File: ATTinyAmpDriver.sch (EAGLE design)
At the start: 22 parts, among them Q1 BSP100, U1 SPX5205M5-L-3-3, U2 ATTINY5-TSHR, U3 MCP6001, X1 DIODES, X2 INPUT

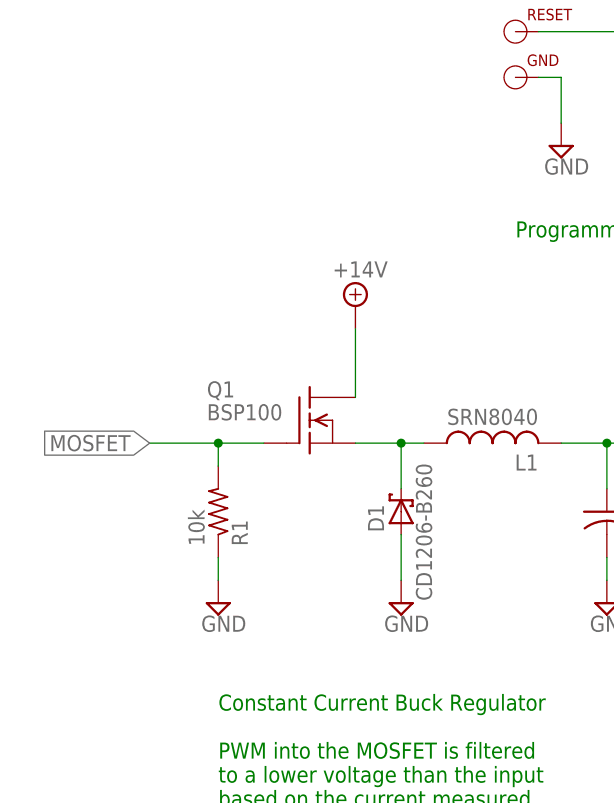
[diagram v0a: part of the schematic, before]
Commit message: P Channel MOSFET
Changed from Incorrect N-Channel to P-Channel High side switch on the
Driver Circuit.
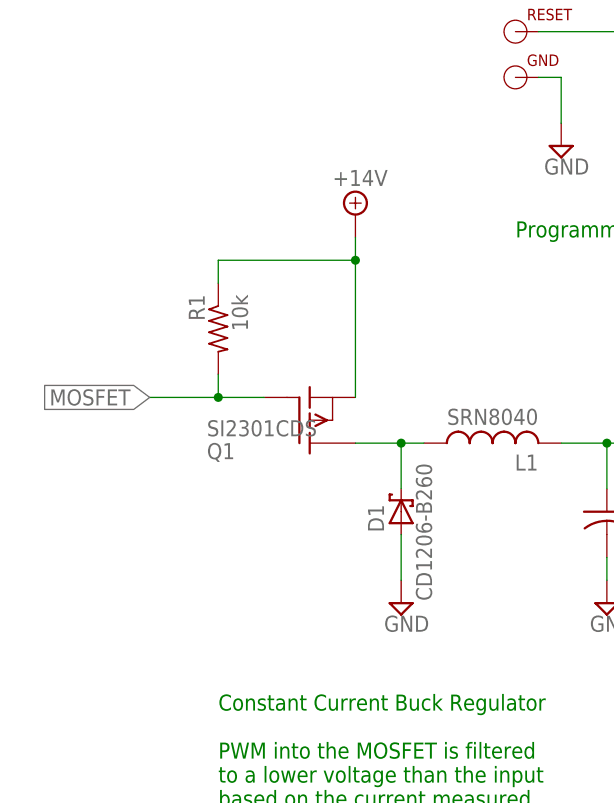
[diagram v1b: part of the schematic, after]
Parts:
- Q1: value BSP100 -> SI2301CDS; device Personal:BSP100 -> Combined:SI2301CDS
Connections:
- net +14V: now also Q1.S, R1.1; no longer Q1.D
- net GND: no longer R1.1
- net L+: now also Q1.D; no longer Q1.S
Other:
- moved on the sheet: Q1, R1
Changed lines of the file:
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@@
 <part name="SUPPLY8" library="supply2" deviceset="GND" device=""/>
 <part name="X1" library="con-phoenix-254" deviceset="MPT2" device="" value="DIODES"/>
-<part name="Q1" library="Personal" deviceset="BSP100" device="">
+<part name="Q1" library="Combined" deviceset="SI2301CDS" device="">
 <attribute name="DIGIKEY" value="568-6956-1-ND"/>
 <attribute name="DIGIKEY_COST" value=".69"/>
@@
 <attribute name="DIGIKEY_COST" value=".05"/>
 </part>
-<part name="SUPPLY14" library="supply2" deviceset="GND" device=""/>
 <part name="TPIDATA" library="Personal" deviceset="TPI" device=""/>
 <part name="TPICLK" library="Personal" deviceset="TPI" device=""/>
@@
 <instance part="X1" gate="-1" x="116.84" y="68.58"/>
 <instance part="X1" gate="-2" x="116.84" y="60.96"/>
-<instance part="Q1" gate="G$1" x="66.04" y="71.12">
-<attribute name="DIGIKEY" x="66.04" y="71.12" size="1.778" layer="96" display="off"/>
-<attribute name="DIGIKEY_COST" x="66.04" y="71.12" size="1.778" layer="96" display="off"/>
-</instance>
-<instance part="SUPPLY11" gate="G$1" x="71.12" y="83.82"/>
+<instance part="Q1" gate="G$1" x="66.04" y="71.12" rot="MR180">
+<attribute name="DIGIKEY" x="66.04" y="71.12" size="1.778" layer="96" rot="MR180" display="off"/>
+<attribute name="DIGIKEY_COST" x="66.04" y="71.12" size="1.778" layer="96" rot="MR180" display="off"/>
+</instance>
+<instance part="SUPPLY11" gate="G$1" x="71.12" y="93.98"/>
 <instance part="U2" gate="A" x="187.96" y="182.88">
 <attribute name="DIGIKEY" x="187.96" y="182.88" size="1.778" layer="96" display="off"/>
@@
 </instance>
 <instance part="SUPPLY13" gate="GND" x="99.06" y="50.8"/>
-<instance part="R1" gate="G$1" x="55.88" y="60.96" rot="MR90">
-<attribute name="DIGIKEY" x="55.88" y="60.96" size="1.778" layer="96" rot="MR90" display="off"/>
-<attribute name="DIGIKEY_COST" x="55.88" y="60.96" size="1.778" layer="96" rot="MR90" display="off"/>
-</instance>
-<instance part="SUPPLY14" gate="GND" x="55.88" y="50.8"/>
+<instance part="R1" gate="G$1" x="55.88" y="81.28" rot="MR270">
+<attribute name="DIGIKEY" x="55.88" y="81.28" size="1.778" layer="96" rot="MR270" display="off"/>
+<attribute name="DIGIKEY_COST" x="55.88" y="81.28" size="1.778" layer="96" rot="MR270" display="off"/>
+</instance>
 <instance part="TPIDATA" gate="G$1" x="88.9" y="124.46"/>
 <instance part="TPICLK" gate="G$1" x="88.9" y="119.38"/>
@@
 </segment>
 <segment>
-<pinref part="R1" gate="G$1" pin="1"/>
-<pinref part="SUPPLY14" gate="GND" pin="GND"/>
-<wire x1="55.88" y1="55.88" x2="55.88" y2="53.34" width="0.1524" layer="91"/>
-</segment>
-<segment>
 <pinref part="GND" gate="G$1" pin="TPI_PIN"/>
 <pinref part="SUPPLY16" gate="GND" pin="GND"/>
@@
 </segment>
 <segment>
-<pinref part="Q1" gate="G$1" pin="D"/>
 <pinref part="SUPPLY11" gate="G$1" pin="+14V"/>
-<wire x1="71.12" y1="73.66" x2="71.12" y2="81.28" width="0.1524" layer="91"/>
+<pinref part="Q1" gate="G$1" pin="S"/>
+<wire x1="71.12" y1="91.44" x2="71.12" y2="88.9" width="0.1524" layer="91"/>
+<pinref part="R1" gate="G$1" pin="1"/>
+<wire x1="71.12" y1="88.9" x2="71.12" y2="73.66" width="0.1524" layer="91"/>
+<wire x1="55.88" y1="86.36" x2="55.88" y2="88.9" width="0.1524" layer="91"/>
+<wire x1="55.88" y1="88.9" x2="71.12" y2="88.9" width="0.1524" layer="91"/>
+<junction x="71.12" y="88.9"/>
 </segment>
 </net>
@@
 <net name="MOSFET" class="0">
 <segment>
+<label x="48.26" y="73.66" size="1.778" layer="95" rot="R180" xref="yes"/>
+<pinref part="R1" gate="G$1" pin="2"/>
+<wire x1="55.88" y1="73.66" x2="48.26" y2="73.66" width="0.1524" layer="91"/>
+<wire x1="55.88" y1="76.2" x2="55.88" y2="73.66" width="0.1524" layer="91"/>
 <pinref part="Q1" gate="G$1" pin="G"/>
-<wire x1="60.96" y1="68.58" x2="55.88" y2="68.58" width="0.1524" layer="91"/>
-<label x="48.26" y="68.58" size="1.778" layer="95" rot="R180" xref="yes"/>
-<pinref part="R1" gate="G$1" pin="2"/>
-<wire x1="55.88" y1="68.58" x2="48.26" y2="68.58" width="0.1524" layer="91"/>
-<wire x1="55.88" y1="66.04" x2="55.88" y2="68.58" width="0.1524" layer="91"/>
-<junction x="55.88" y="68.58"/>
+<wire x1="60.96" y1="73.66" x2="55.88" y2="73.66" width="0.1524" layer="91"/>
+<junction x="55.88" y="73.66"/>
 </segment>
 <segment>
@@
 <pinref part="D1" gate="G$1" pin="C"/>
 <wire x1="76.2" y1="63.5" x2="76.2" y2="68.58" width="0.1524" layer="91"/>
-<pinref part="Q1" gate="G$1" pin="S"/>
-<wire x1="71.12" y1="68.58" x2="76.2" y2="68.58" width="0.1524" layer="91"/>
 <pinref part="L1" gate="G$1" pin="1"/>
 <wire x1="78.74" y1="68.58" x2="76.2" y2="68.58" width="0.1524" layer="91"/>
+<pinref part="Q1" gate="G$1" pin="D"/>
+<wire x1="71.12" y1="68.58" x2="76.2" y2="68.58" width="0.1524" layer="91"/>
 <junction x="76.2" y="68.58"/>
 </segment>

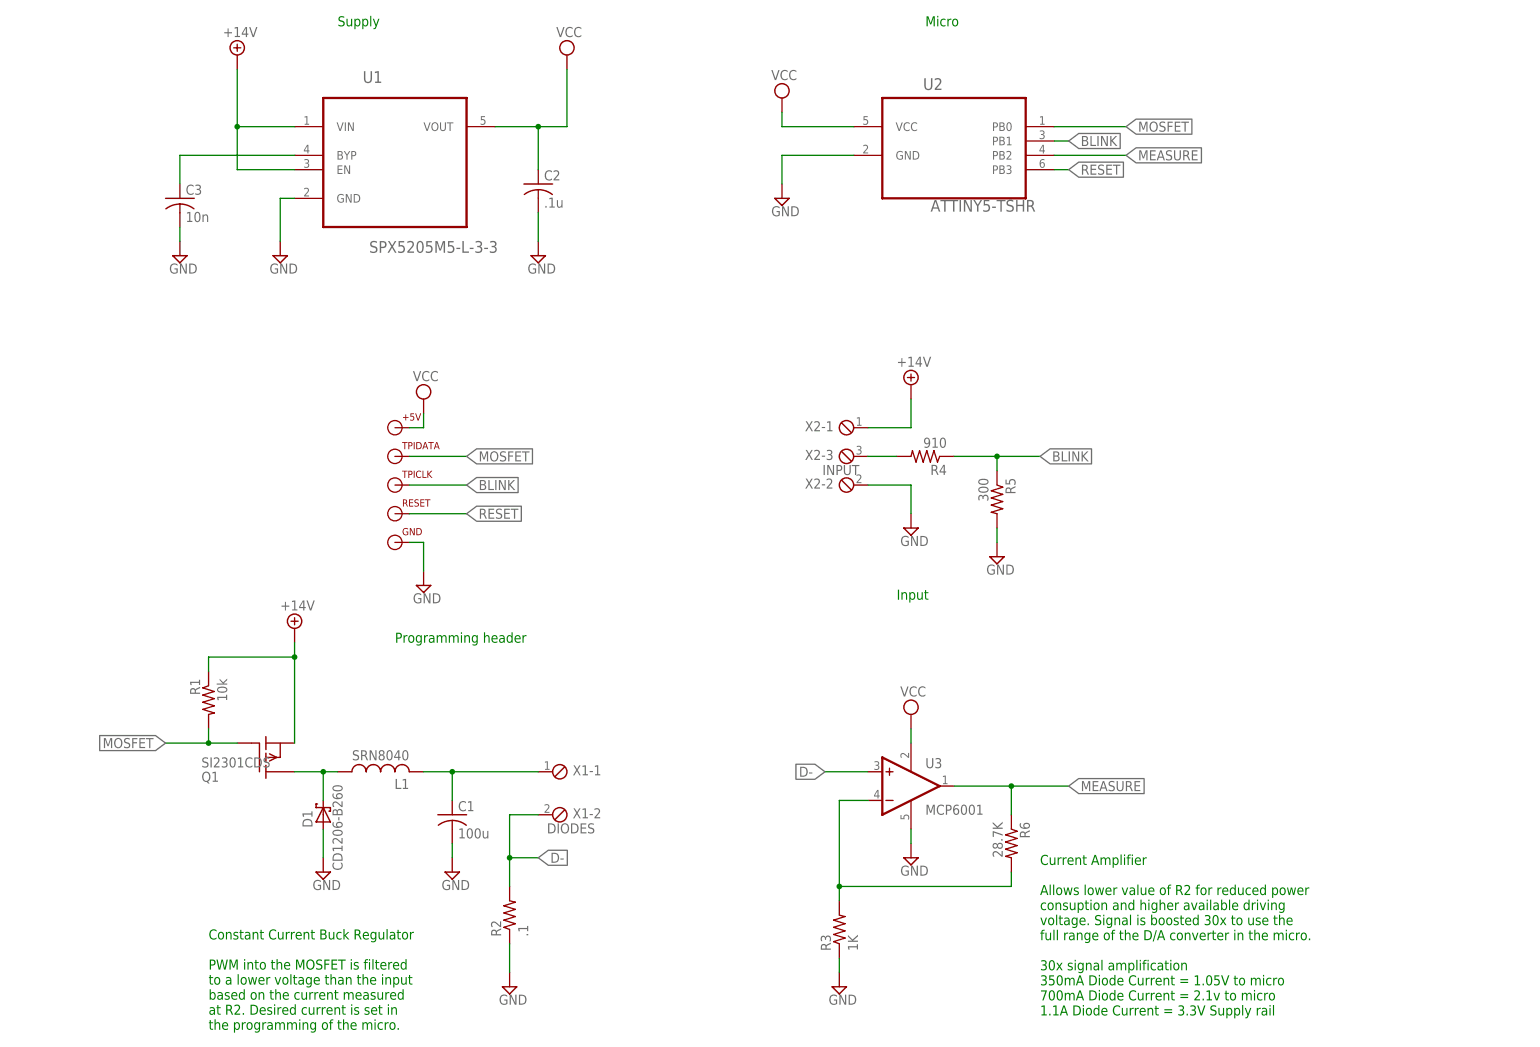
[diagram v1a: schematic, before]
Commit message: Added Driving transistor for P-FET
Added driver transistor to P Channel MOSFET and capacitor to op-amp
output.
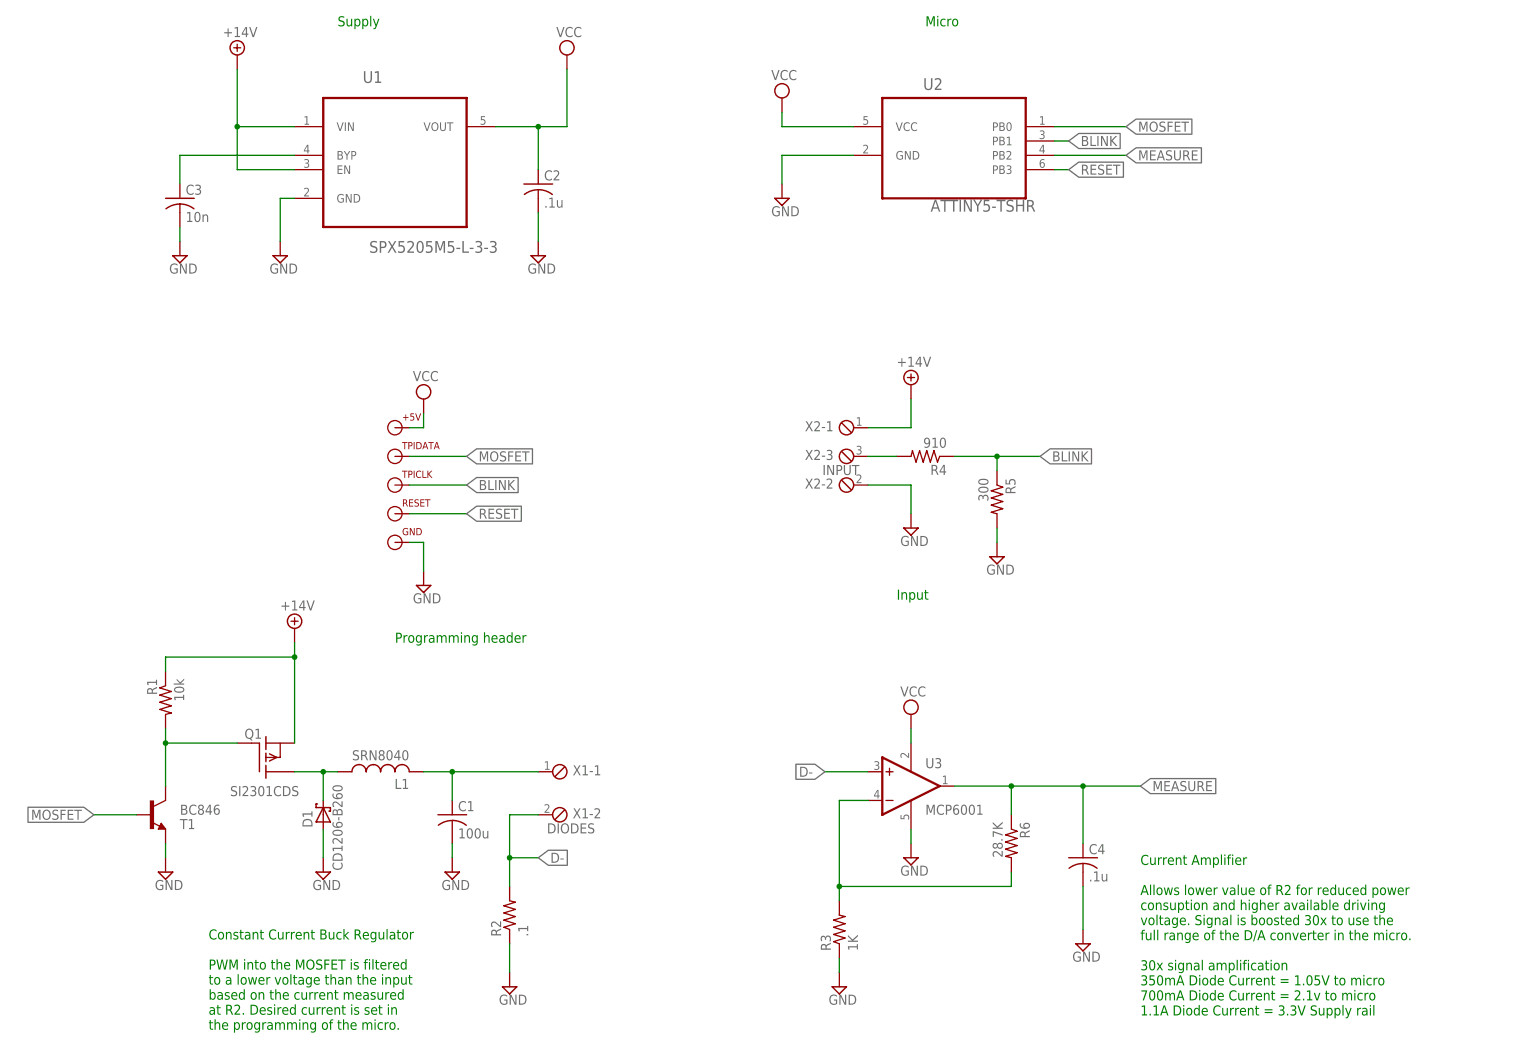
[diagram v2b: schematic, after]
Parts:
- added C4: .1u, resistor:C-USC0805
- added T1: BC846, transistor-neu-to92:BC846
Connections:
- new net N$5: Q1.G, R1.2, T1.C
- net GND: now also C4.2, T1.E
- net MEASURE: now also C4.1
- net MOSFET: now also T1.B; no longer Q1.G, R1.2
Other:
- moved on the sheet: R1
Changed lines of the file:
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@@
 <attribute name="DIGIKEY_COST" value=".04"/>
 </part>
+<part name="T1" library="transistor-neu-to92" deviceset="BC846" device=""/>
+<part name="SUPPLY14" library="supply2" deviceset="GND" device=""/>
+<part name="C4" library="resistor" deviceset="C-US" device="C0805" value=".1u">
+<attribute name="DIGIKEY" value="445-7534-1-ND"/>
+<attribute name="DIGIKEY_COST" value=".10"/>
+</part>
+<part name="SUPPLY18" library="supply2" deviceset="GND" device=""/>
 </parts>
 <sheets>
@@
 <text x="177.8" y="99.06" size="1.778" layer="91">Input</text>
 <text x="88.9" y="91.44" size="1.778" layer="91">Programming header</text>
-<text x="203.2" y="25.4" size="1.778" layer="91">Current Amplifier
+<text x="220.98" y="25.4" size="1.778" layer="91">Current Amplifier
 Allows lower value of R2 for reduced power
 consuption and higher available driving
@@
 <instance part="X1" gate="-1" x="116.84" y="68.58"/>
 <instance part="X1" gate="-2" x="116.84" y="60.96"/>
-<instance part="Q1" gate="G$1" x="66.04" y="71.12" rot="MR180">
+<instance part="Q1" gate="G$1" x="66.04" y="71.12" smashed="yes" rot="MR180">
 <attribute name="DIGIKEY" x="66.04" y="71.12" size="1.778" layer="96" rot="MR180" display="off"/>
 <attribute name="DIGIKEY_COST" x="66.04" y="71.12" size="1.778" layer="96" rot="MR180" display="off"/>
+<attribute name="VALUE" x="59.69" y="66.04" size="1.778" layer="96" rot="MR180"/>
+<attribute name="NAME" x="62.23" y="76.2" size="1.778" layer="95" rot="MR180"/>
 </instance>
 <instance part="SUPPLY11" gate="G$1" x="71.12" y="93.98"/>
@@
 </instance>
 <instance part="SUPPLY13" gate="GND" x="99.06" y="50.8"/>
-<instance part="R1" gate="G$1" x="55.88" y="81.28" rot="MR270">
-<attribute name="DIGIKEY" x="55.88" y="81.28" size="1.778" layer="96" rot="MR270" display="off"/>
-<attribute name="DIGIKEY_COST" x="55.88" y="81.28" size="1.778" layer="96" rot="MR270" display="off"/>
+<instance part="R1" gate="G$1" x="48.26" y="81.28" rot="MR270">
+<attribute name="DIGIKEY" x="48.26" y="81.28" size="1.778" layer="96" rot="MR270" display="off"/>
+<attribute name="DIGIKEY_COST" x="48.26" y="81.28" size="1.778" layer="96" rot="MR270" display="off"/>
 </instance>
 <instance part="TPIDATA" gate="G$1" x="88.9" y="124.46"/>
@@
 <attribute name="DIGIKEY_COST" x="198.12" y="55.88" size="1.778" layer="96" rot="R270" display="off"/>
 </instance>
+<instance part="T1" gate="G$1" x="45.72" y="60.96" smashed="yes">
+<attribute name="NAME" x="50.8" y="58.42" size="1.778" layer="95"/>
+<attribute name="VALUE" x="50.8" y="60.96" size="1.778" layer="96"/>
+</instance>
+<instance part="SUPPLY14" gate="GND" x="48.26" y="50.8"/>
+<instance part="C4" gate="G$1" x="210.82" y="53.34">
+<attribute name="DIGIKEY" x="210.82" y="53.34" size="1.778" layer="96" display="off"/>
+<attribute name="DIGIKEY_COST" x="210.82" y="53.34" size="1.778" layer="96" display="off"/>
+</instance>
+<instance part="SUPPLY18" gate="GND" x="210.82" y="38.1"/>
 </instances>
 <busses>
@@
 <pinref part="SUPPLY19" gate="GND" pin="GND"/>
 <wire x1="167.64" y1="35.56" x2="167.64" y2="33.02" width="0.1524" layer="91"/>
+</segment>
+<segment>
+<pinref part="T1" gate="G$1" pin="E"/>
+<pinref part="SUPPLY14" gate="GND" pin="GND"/>
+<wire x1="48.26" y1="55.88" x2="48.26" y2="53.34" width="0.1524" layer="91"/>
+</segment>
+<segment>
+<pinref part="C4" gate="G$1" pin="2"/>
+<pinref part="SUPPLY18" gate="GND" pin="GND"/>
+<wire x1="210.82" y1="48.26" x2="210.82" y2="40.64" width="0.1524" layer="91"/>
 </segment>
 </net>
@@
 <pinref part="R1" gate="G$1" pin="1"/>
 <wire x1="71.12" y1="88.9" x2="71.12" y2="73.66" width="0.1524" layer="91"/>
-<wire x1="55.88" y1="86.36" x2="55.88" y2="88.9" width="0.1524" layer="91"/>
-<wire x1="55.88" y1="88.9" x2="71.12" y2="88.9" width="0.1524" layer="91"/>
+<wire x1="48.26" y1="86.36" x2="48.26" y2="88.9" width="0.1524" layer="91"/>
+<wire x1="48.26" y1="88.9" x2="71.12" y2="88.9" width="0.1524" layer="91"/>
 <junction x="71.12" y="88.9"/>
 </segment>
@@
 <segment>
 <wire x1="187.96" y1="66.04" x2="198.12" y2="66.04" width="0.1524" layer="91"/>
-<label x="208.28" y="66.04" size="1.778" layer="95" rot="MR180" xref="yes"/>
+<label x="220.98" y="66.04" size="1.778" layer="95" rot="MR180" xref="yes"/>
 <pinref part="U3" gate="G$1" pin="OUT"/>
 <pinref part="R6" gate="G$1" pin="1"/>
-<wire x1="198.12" y1="66.04" x2="208.28" y2="66.04" width="0.1524" layer="91"/>
+<wire x1="198.12" y1="66.04" x2="210.82" y2="66.04" width="0.1524" layer="91"/>
+<wire x1="210.82" y1="66.04" x2="220.98" y2="66.04" width="0.1524" layer="91"/>
 <wire x1="198.12" y1="60.96" x2="198.12" y2="66.04" width="0.1524" layer="91"/>
 <junction x="198.12" y="66.04"/>
+<pinref part="C4" gate="G$1" pin="1"/>
+<wire x1="210.82" y1="55.88" x2="210.82" y2="66.04" width="0.1524" layer="91"/>
+<junction x="210.82" y="66.04"/>
 </segment>
 <segment>
@@
 <net name="MOSFET" class="0">
 <segment>
-<label x="48.26" y="73.66" size="1.778" layer="95" rot="R180" xref="yes"/>
-<pinref part="R1" gate="G$1" pin="2"/>
-<wire x1="55.88" y1="73.66" x2="48.26" y2="73.66" width="0.1524" layer="91"/>
-<wire x1="55.88" y1="76.2" x2="55.88" y2="73.66" width="0.1524" layer="91"/>
-<pinref part="Q1" gate="G$1" pin="G"/>
-<wire x1="60.96" y1="73.66" x2="55.88" y2="73.66" width="0.1524" layer="91"/>
-<junction x="55.88" y="73.66"/>
-</segment>
-<segment>
 <wire x1="205.74" y1="182.88" x2="218.44" y2="182.88" width="0.1524" layer="91"/>
 <label x="218.44" y="182.88" size="1.778" layer="95" xref="yes"/>
@@
 <wire x1="91.44" y1="124.46" x2="101.6" y2="124.46" width="0.1524" layer="91"/>
 <label x="101.6" y="124.46" size="1.778" layer="95" xref="yes"/>
+</segment>
+<segment>
+<pinref part="T1" gate="G$1" pin="B"/>
+<wire x1="35.56" y1="60.96" x2="43.18" y2="60.96" width="0.1524" layer="91"/>
+<label x="35.56" y="60.96" size="1.778" layer="95" rot="R180" xref="yes"/>
 </segment>
 </net>
@@
 </segment>
 </net>
+<net name="N$5" class="0">
+<segment>
+<pinref part="Q1" gate="G$1" pin="G"/>
+<pinref part="T1" gate="G$1" pin="C"/>
+<wire x1="60.96" y1="73.66" x2="48.26" y2="73.66" width="0.1524" layer="91"/>
+<wire x1="48.26" y1="73.66" x2="48.26" y2="66.04" width="0.1524" layer="91"/>
+<pinref part="R1" gate="G$1" pin="2"/>
+<wire x1="48.26" y1="76.2" x2="48.26" y2="73.66" width="0.1524" layer="91"/>
+<junction x="48.26" y="73.66"/>
+</segment>
+</net>
